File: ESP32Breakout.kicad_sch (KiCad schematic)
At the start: 17 parts, among them J4 USB_C_Receptacle_USB2.0_16P, SW1 PTS636SM43SMTR LFS, SW2 PTS636SM43SMTR LFS, U6 ESP32-S3-WROOM-1U

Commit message: add capacitor and resistor footprints
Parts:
- removed C12: 22uF, Capacitor_SMD:C_1206_3216Metric, symbol Device:C_Small
- removed C14: 1μF, Capacitor_SMD:C_0402_1005Metric, symbol Device:C_Small
- removed C16: 0.1uF, Capacitor_SMD:C_0402_1005Metric, symbol Device:C_Small
- added C22: 22uF, Capacitor_SMD:C_0805_2012Metric, symbol Device:C_Small
- added C24: 1uF, Capacitor_SMD:C_0603_1608Metric, symbol Device:C_Small
- added C26: 0.1μF, Capacitor_SMD:C_0402_1005Metric, symbol Device:C_Small
- C23: renamed from C13; LCSC C1525 -> C307331
- C25: renamed from C15; LCSC C1525 -> C307331
- J4: footprint Connector_USB:USB_C_Receptacle_HCTL_HC-TYPE-C-16P-01A -> Connector_USB:USB_C_Receptacle_G-Switch_GT-USB-7010ASV; LCSC (none) -> C2988369
- SW1, SW2: value PTS636SM43SMTR LFS -> USAKRO UK-B0227-G4.3-B-250; LCSC (none) -> C556661
- renumbered R27 to R30, R28 to R31, R29 to R32, R30 to R33, R31 to R34, R32 to R35, U6 to U7
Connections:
- net +3.3V: now also C22.1
- net 5V_USB: now also C26.1
- net GND: now also C22.2, C24.2, C26.2
- net I2C_SCL: now also U7.22 (IO14); no longer U7.26 (IO45)
- net I2C_SDA: now also U7.23 (IO21); no longer U7.25 (IO48)
- net RESET: now also C24.1
- net WIFI_IND: now also U7.26 (IO45); no longer U7.21 (IO13)
- new net DRDY5: U7.21 (IO13)
- new net POWER_GOOD: U7.25 (IO48)
- no-connect marks 18 -> 16

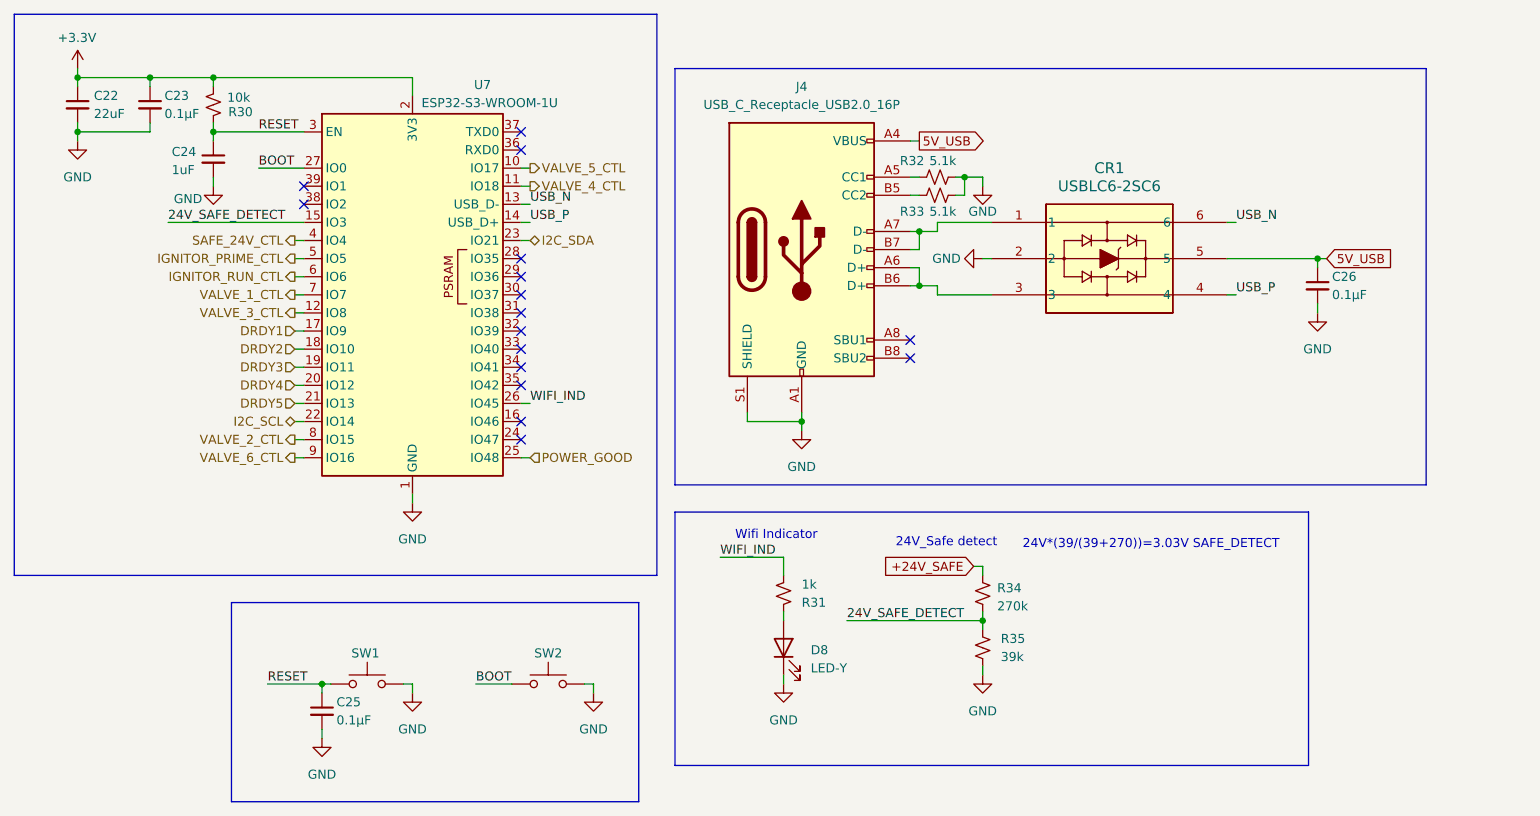
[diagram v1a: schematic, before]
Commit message: change connectors and more progress on pcb
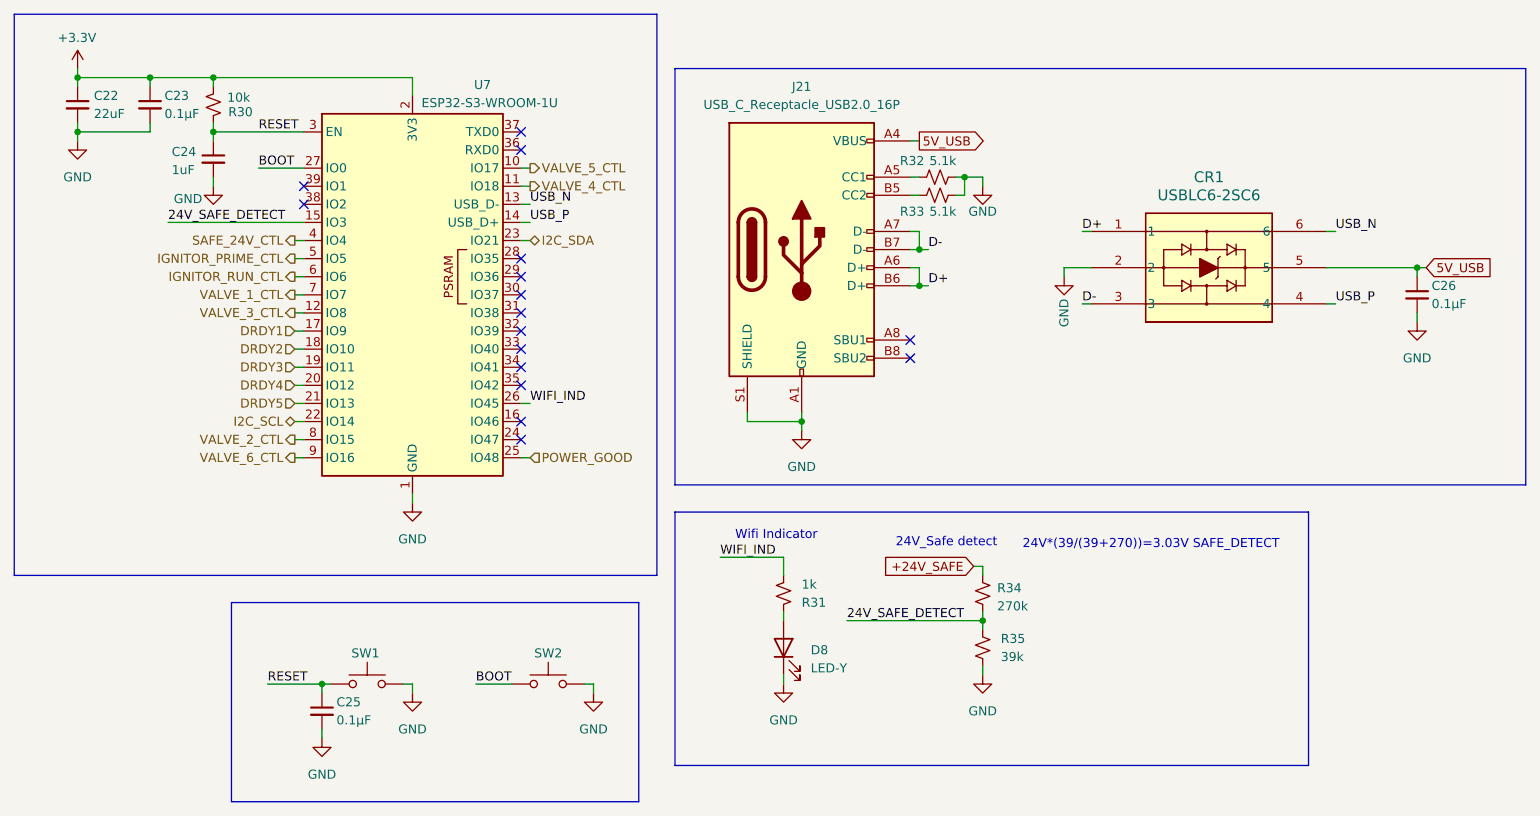
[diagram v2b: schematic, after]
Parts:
- removed J4: USB_C_Receptacle_USB2.0_16P, Connector_USB:USB_C_Receptacle_G-Switch_GT-USB-7010ASV, symbol Connector:USB_C_Receptacle_USB2.0_16P
- added J21: USB_C_Receptacle_USB2.0_16P, Connector_USB:USB_C_Receptacle_G-Switch_GT-USB-7051x, symbol Connector:USB_C_Receptacle_USB2.0_16P
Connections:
- net 5V_USB: now also J21.A4 (VBUS), J21.A9 (VBUS), J21.B4 (VBUS), J21.B9 (VBUS)
- net GND: now also J21.A1 (GND), J21.A12 (GND), J21.B1 (GND), J21.B12 (GND), J21.S1 (SHIELD)
- net at R32.1: now also J21.A5 (CC1)
- net at R33.1: now also J21.B5 (CC2)
- net D-: now reaches CR1.3
- net D-: now also J21.A7 (D-), J21.B7 (D-)
- net D+: now reaches CR1.1
- net D+: now also J21.A6 (D+), J21.B6 (D+)
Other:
- moved on the sheet: C26, CR1

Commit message: change clamping resistors on tc adcs for lower leakage current
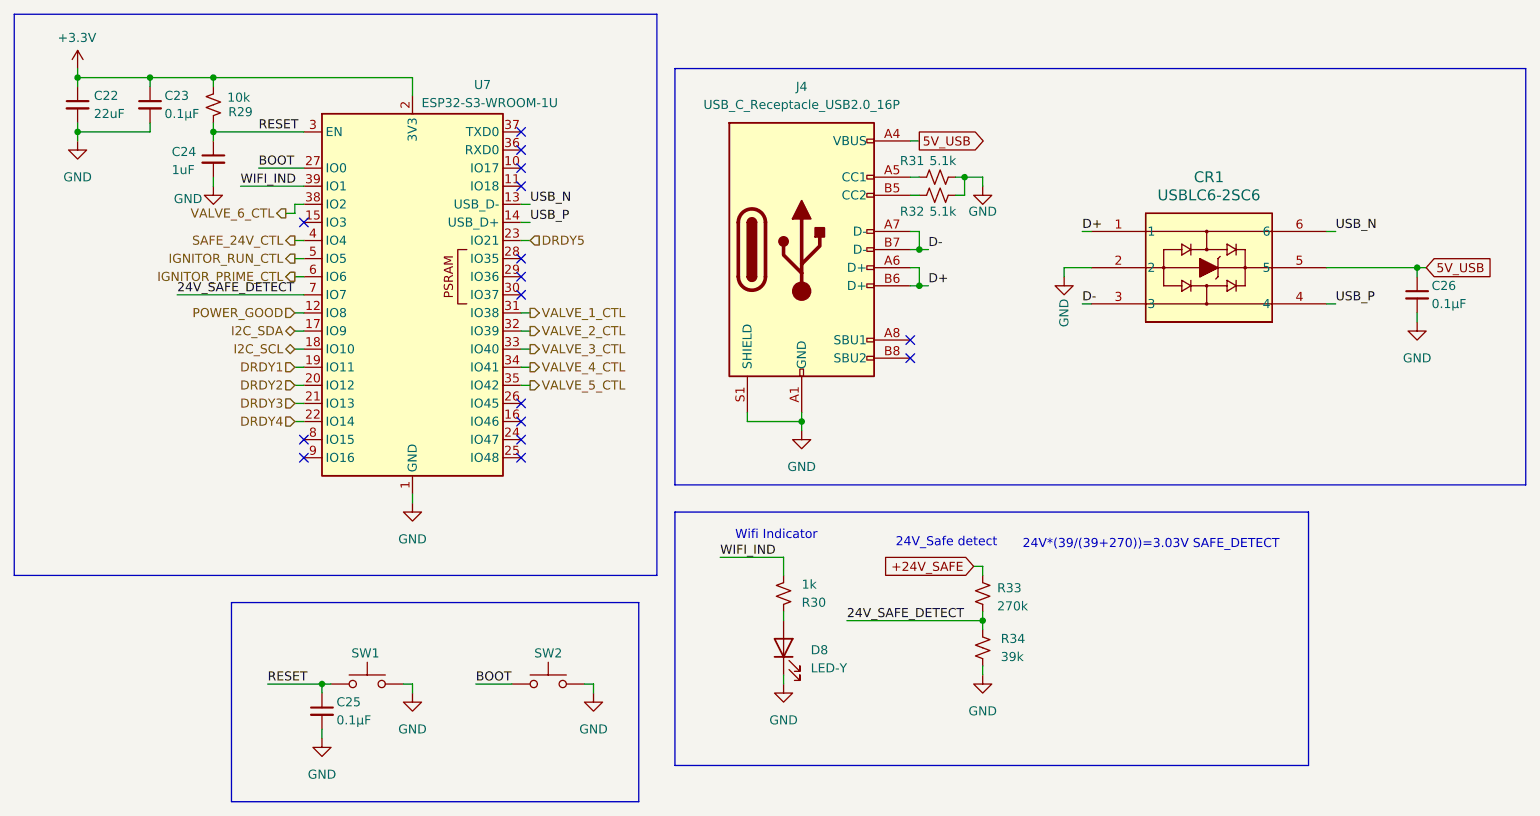
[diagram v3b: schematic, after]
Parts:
- renumbered J21 to J4, R30 to R29, R31 to R30, R32 to R31, R33 to R32, R34 to R33, R35 to R34
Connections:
- net 24V_SAFE_DETECT: now also U7.7 (IO7); no longer U7.15 (IO3)
- net DRDY1: now also U7.19 (IO11); no longer U7.17 (IO9)
- net DRDY2: now also U7.20 (IO12); no longer U7.18 (IO10)
- net DRDY3: now also U7.21 (IO13); no longer U7.19 (IO11)
- net DRDY4: now also U7.22 (IO14); no longer U7.20 (IO12)
- net DRDY5: now also U7.23 (IO21); no longer U7.21 (IO13)
- net I2C_SCL: now also U7.18 (IO10); no longer U7.22 (IO14)
- net I2C_SDA: now also U7.17 (IO9); no longer U7.23 (IO21)
- net IGNITOR_PRIME_CTL: now also U7.6 (IO6); no longer U7.5 (IO5)
- net IGNITOR_RUN_CTL: now also U7.5 (IO5); no longer U7.6 (IO6)
- net POWER_GOOD: now also U7.12 (IO8); no longer U7.25 (IO48)
- net VALVE_1_CTL: now also U7.31 (IO38); no longer U7.7 (IO7)
- net VALVE_2_CTL: now also U7.32 (IO39); no longer U7.8 (IO15)
- net VALVE_3_CTL: now also U7.33 (IO40); no longer U7.12 (IO8)
- net VALVE_4_CTL: now also U7.34 (IO41); no longer U7.11 (IO18)
- net VALVE_5_CTL: now also U7.35 (IO42); no longer U7.10 (IO17)
- net VALVE_6_CTL: now also U7.38 (IO2); no longer U7.9 (IO16)
- net WIFI_IND: now also U7.39 (IO1); no longer U7.26 (IO45)

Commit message: Update version number in KiCad files
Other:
- title: ESP32 Interface -> PANDA
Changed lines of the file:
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@@
 	(paper "A4")
 	(title_block
-		(title "ESP32 Interface")
-		(rev "1.0.0")
+		(title "PANDA")
+		(date "2025-12-21")
+		(rev "3.0.0")
 		(company "Queen's Rocket Engineering Team")
 	)
